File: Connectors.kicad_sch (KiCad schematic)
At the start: 4 parts, among them J1 Conn_01x04_Pin, J2 Conn_01x04_Pin, J3 Conn_01x09_Pin, J4 Conn_02x03_Odd_Even

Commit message: add footprints to symbols
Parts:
- J1, J2: footprint (none) -> Connector_PinHeader_2.54mm:PinHeader_1x04_P2.54mm_Vertical
- J3: footprint (none) -> Connector_PinHeader_2.54mm:PinHeader_1x09_P2.54mm_Vertical
- J4: footprint (none) -> Connector_PinHeader_2.54mm:PinHeader_2x03_P2.54mm_Vertical
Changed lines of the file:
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@@
 			)
 		)
-		(property "Footprint" ""
+		(property "Footprint" "Connector_PinHeader_2.54mm:PinHeader_2x03_P2.54mm_Vertical"
 			(at 212.09 104.14 0)
 			(effects
@@
 			)
 		)
-		(property "Footprint" ""
+		(property "Footprint" "Connector_PinHeader_2.54mm:PinHeader_1x04_P2.54mm_Vertical"
 			(at 189.23 72.39 0)
 			(effects
@@
 			)
 		)
-		(property "Footprint" ""
+		(property "Footprint" "Connector_PinHeader_2.54mm:PinHeader_1x04_P2.54mm_Vertical"
 			(at 209.55 72.39 0)
 			(effects
@@
 			)
 		)
-		(property "Footprint" ""
+		(property "Footprint" "Connector_PinHeader_2.54mm:PinHeader_1x09_P2.54mm_Vertical"
 			(at 190.5 104.14 0)
 			(effects

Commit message: Wiring completed
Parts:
- renumbered J3 to J2, J2 to J3
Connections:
- net MISO: now reaches J4.1 (Pin_1)
- net Vcc: now reaches J4.2 (Pin_2)
- net Vcc: now also J1.2 (Pin_2), J2.9 (Pin_9), J3.2 (Pin_2)
- net SCK: now reaches J4.3 (Pin_3)
- net SCK: now also J1.4 (Pin_4)
- net MOSI: now reaches J4.4 (Pin_4)
- net RESET: now reaches J4.5 (Pin_5)
- net GND: now reaches J4.6 (Pin_6)
- net GND: now also J1.1 (Pin_1), J2.8 (Pin_8), J3.1 (Pin_1)
- net SDA: now reaches J1.3 (Pin_3)
- net RX: now reaches J3.3 (Pin_3)
- net TX: now reaches J3.4 (Pin_4)
- net D2: now reaches J2.1 (Pin_1)
- net D3: now reaches J2.2 (Pin_2)
- net D4: now reaches J2.3 (Pin_3)
- net D5: now reaches J2.4 (Pin_4)
- net D6: now reaches J2.5 (Pin_5)
- net D7: now reaches J2.6 (Pin_6)
- net D8: now reaches J2.7 (Pin_7)
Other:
- moved on the sheet: J2, J3, J4

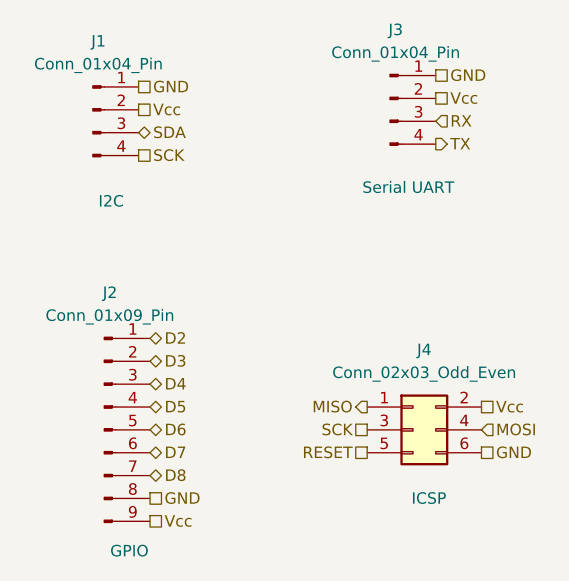
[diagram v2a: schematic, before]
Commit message: fixed 2 defects in schematic
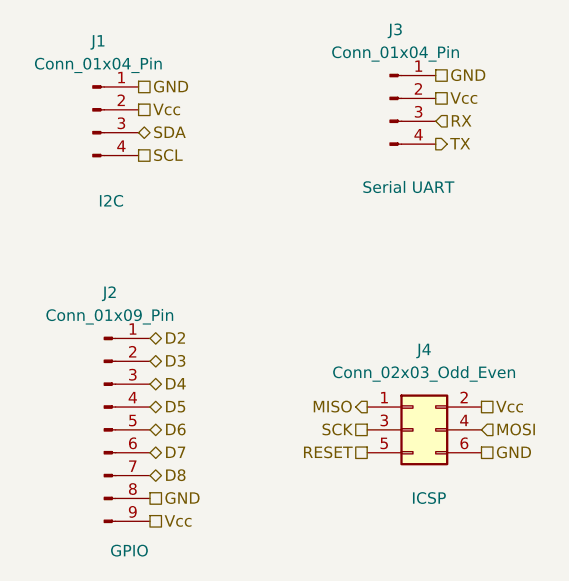
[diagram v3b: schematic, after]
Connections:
- net SCK: no longer J1.4 (Pin_4)
- new net SCL: J1.4 (Pin_4)
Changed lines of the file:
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@@
 		)
 	)
-	(hierarchical_label "SCK"
+	(hierarchical_label "SCL"
 		(shape passive)
 		(at 194.31 77.47 0)
